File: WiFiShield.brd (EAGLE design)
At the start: 69.2 x 53.3 mm, 39 parts, among them IC1 MIC5219-3.3YM5, IC2 CC3000, J7 Arduino-compatible headers, Q1 2N7002, Q2 2N7002, Q3 2N7002, Q4 2N7002, Q5 2N7002

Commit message: foo
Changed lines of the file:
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@@
 <via x="33.02" y="39.37" extent="1-16" drill="0.4"/>
 <wire x1="33.02" y1="39.37" x2="55.08625" y2="39.37" width="0.4064" layer="16"/>
-<wire x1="55.08625" y1="39.37" x2="56.67375" y2="37.7825" width="0.2032" layer="16"/>
+<wire x1="55.08625" y1="39.37" x2="56.67375" y2="37.7825" width="0.254" layer="16"/>
 <wire x1="57.045" y1="36.46" x2="57.045" y2="37.41125" width="0.2032" layer="1"/>
 <wire x1="57.045" y1="37.41125" x2="56.67375" y2="37.7825" width="0.2032" layer="1"/>
@@
 <wire x1="39.6875" y1="41.5425" x2="39.685" y2="41.545" width="0.4064" layer="1"/>
 <wire x1="39.497" y1="39.37" x2="56.67375" y2="39.37" width="0.4064" layer="1"/>
-<wire x1="56.67375" y1="39.37" x2="58.245" y2="37.79875" width="0.2032" layer="16"/>
+<wire x1="56.67375" y1="39.37" x2="58.245" y2="37.79875" width="0.254" layer="16"/>
 <wire x1="58.245" y1="36.46" x2="58.245" y2="37.79875" width="0.2032" layer="1"/>
 <via x="56.67375" y="39.37" extent="1-16" drill="0.4"/>

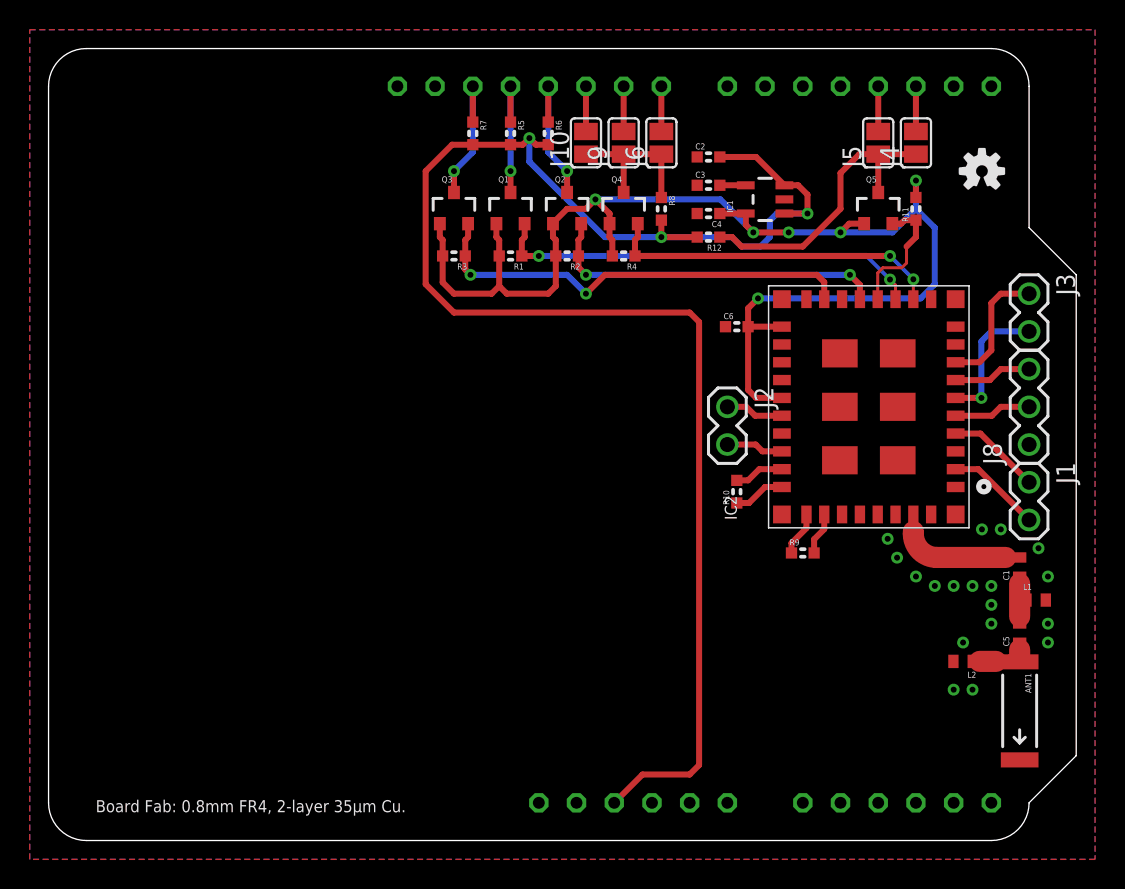
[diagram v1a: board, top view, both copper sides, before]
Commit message: finished silkscreen
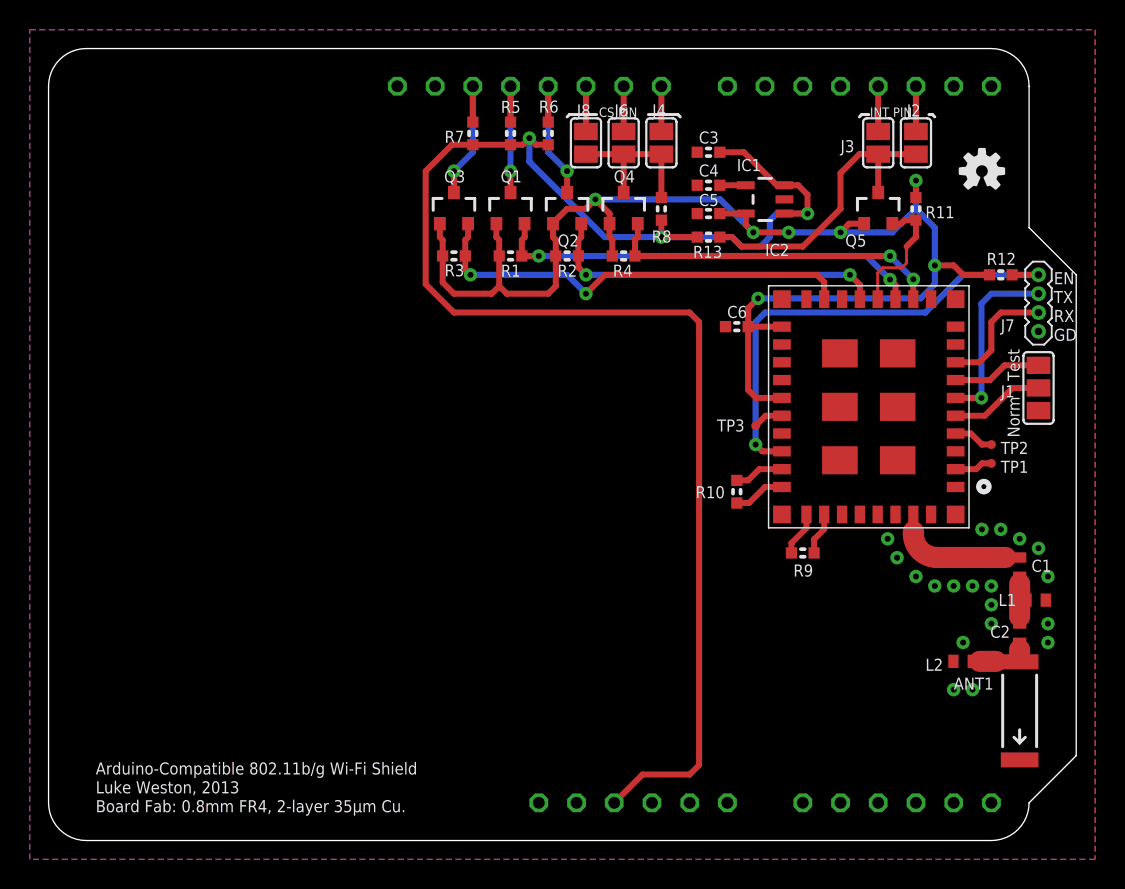
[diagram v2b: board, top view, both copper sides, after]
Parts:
- removed J10, J9: (no value), freetronics-luke:SJ
- added R13: 10kΩ, freetronics-master-v1:0603
- added TP1, TP2, TP3: (no value), testpad:TP06R
- C2: value 2.2µF -> 2.2pF; device freetronics-master-v1:0603 -> freetronics-master-v1:C0402
- C3: value 470pF -> 2.2µF
- C4: value 2.2µF -> 470pF
- C5: value 2.2pF -> 2.2µF; device freetronics-master-v1:C0402 -> freetronics-master-v1:0603
- IC1: value MIC5219-3.3YM5 -> MIC5219
- J1: value (none) -> Mode; device freetronics-master-v1:1X02 -> freetronics-master-v1:SJ_2
- J2, J3: device freetronics-master-v1:1X02 -> freetronics-luke:SJ
- J5: value (none) -> Arduino-compatible headers; device freetronics-luke:SJ -> Arduino-Various:NO-OUTLINE-OCTAGONAL-NOTEXT
- J7: value Arduino-compatible headers -> (none); device Arduino-Various:NO-OUTLINE-OCTAGONAL-NOTEXT -> freetronics-master-v1:1X04-1.27MM
- J8: device freetronics-master-v1:1X03 -> freetronics-luke:SJ
- moved C2 38.3 mm to (65.4, 14.0), turned to 90 degrees
- moved J8 36.1 mm to (36.2, 47.0)
- moved C5 35.2 mm to (44.5, 42.2), turned to 180 degrees
- moved J7 33.6 mm to (66.7, 38.1)
- moved J5 29.6 mm to (35.6, 25.4), turned to 270 degrees
- moved J2 21.8 mm to (58.4, 47.0), turned to 90 degrees
- moved R12 19.8 mm to (64.1, 38.1)
- moved J4 17.1 mm to (41.3, 47.0)
- moved J3 14.4 mm to (55.9, 47.0), turned to 90 degrees
- moved J1 6.38 mm to (66.7, 30.5), turned to 90 degrees
- moved J6 2.54 mm to (38.7, 47.0)
- moved C3 2.22 mm to (44.5, 46.4)
- moved C4 1.91 mm to (44.5, 44.1), turned to 0 degrees
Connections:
- net !CC3000_CS_5V: now also J4.1, J8.1; no longer J10.1, J9.1
- net +3V3: now also C5.1, R12.2; no longer C4.1
- net +5V: now also C3.2, J5.5V, R13.2; no longer C2.2, J7.5V, R12.2
- net 3V3: now also J5.3V3; no longer J7.3V3
- net CC3000_EN: now also J7.1, R12.1; no longer J2.2
- net CC3000_IRQ_5V: now also J2.1, J3.1, R13.1; no longer J4.1, J5.1, R12.1
- net GND: now also C4.1, C5.2, J1.1, J5.GND0, J5.GND1, J5.GND2, J7.4; no longer C2.1, C4.2, J7.GND0, J7.GND1, J7.GND2, J8.1
- net MISO_5V: now also J5.12; no longer J7.12
- net MOSI_5V: now also J5.11; no longer J7.11
- net N$103: now also C2.2; no longer C5.2
- net N$104: now also C2.1; no longer C5.1
- net N$11: now also J5.10, J8.2; no longer J10.2, J7.10
- net N$4: now also J3.2, J5.3; no longer J5.2, J7.3
- net N$43: now also C4.2; no longer C3.2
- net N$6: now also J2.2, J5.2; no longer J4.2, J7.2
- net N$7: now also J5.9, J6.2; no longer J7.9, J9.2
- net N$9: now also J4.2, J5.8; no longer J6.2, J7.8
- net RES_1: now also TP1.TP; no longer J1.2
- net RES_2: now also TP2.TP; no longer J1.1
- net RES_3: now also TP3.TP; no longer J2.1
- net SCK_5V: now also J5.13; no longer J7.13
- net VIN: now also J5.VIN; no longer J7.VIN
- net WL_EN1: now also J1.3; no longer J8.3
- net WL_EN2: now also J1.2; no longer J8.2
- net WL_UART_RX: now also J7.3; no longer J3.1
- net WL_UART_TX: now also J7.2; no longer J3.2
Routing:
- net CC3000_EN: track 3.87 -> 32.4 mm, vias 0 -> 1
- net +3V3: track 89.4 -> 93.4 mm, vias 6 -> 7
- net RES_1: track 6.36 -> 2.57 mm
- net RES_2: track 6.30 -> 2.71 mm
- net WL_UART_TX: track 9.03 -> 12.2 mm
- net RES_3: track 3.92 -> 2.05 mm
- net WL_EN2: track 5.19 -> 6.35 mm
- net WL_EN1: track 5.25 -> 5.99 mm
- net WL_UART_RX: track 8.72 -> 8.08 mm
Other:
- board text added: "Arduino-Compatible 802.11b/g Wi-Fi Shield"
- board text added: "CS PIN"
- board text added: "EN"
- board text added: "GD"
- board text added: "INT PIN"
- board text added: "Luke Weston, 2013"
- board text added: "Norm"
- board text added: "RX"
- board text added: "TX"
- board text added: "Test"

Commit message: tweaked RF layout
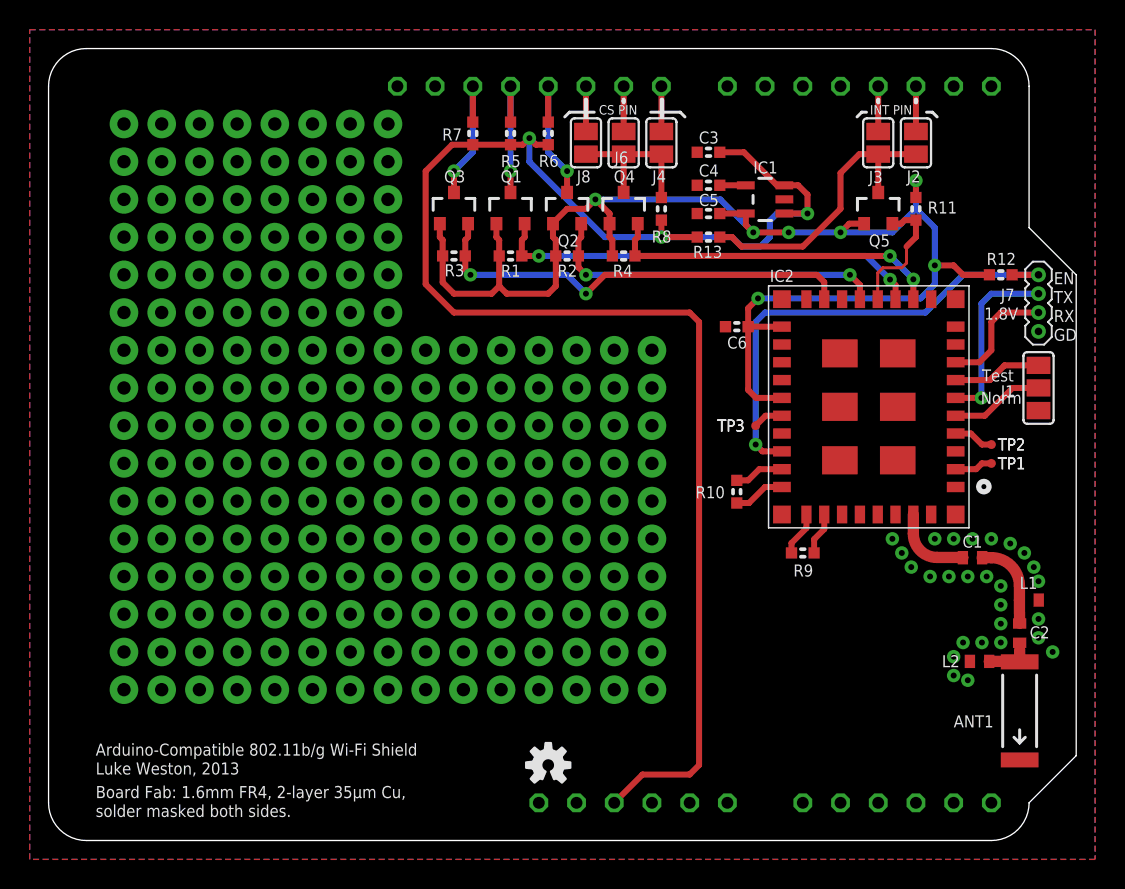
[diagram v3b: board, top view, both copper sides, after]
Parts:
- moved SY 49.5 mm to (33.7, 5.08)
- moved C1 3.24 mm to (62.2, 19.1), turned to 180 degrees
- moved L2 1.11 mm to (62.7, 12.1)
- moved L1 0.48 mm to (66.0, 16.2)
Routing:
- net N$16: track 9.12 -> 5.31 mm
- net N$104: track 5.83 -> 4.00 mm
- net N$103: track 4.45 -> 5.83 mm
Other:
- board text added: "1.8V"
- board text added: "Board Fab: 1.6mm FR4, 2-layer 35µm Cu,"
- board text added: "TP1"
- board text added: "TP2"
- board text added: "TP3"
- board text added: "solder masked both sides."
- board text removed: "Board Fab: 0.8mm FR4, 2-layer 35µm Cu."

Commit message: changed to microstrip antenna, fixed 50Ω line
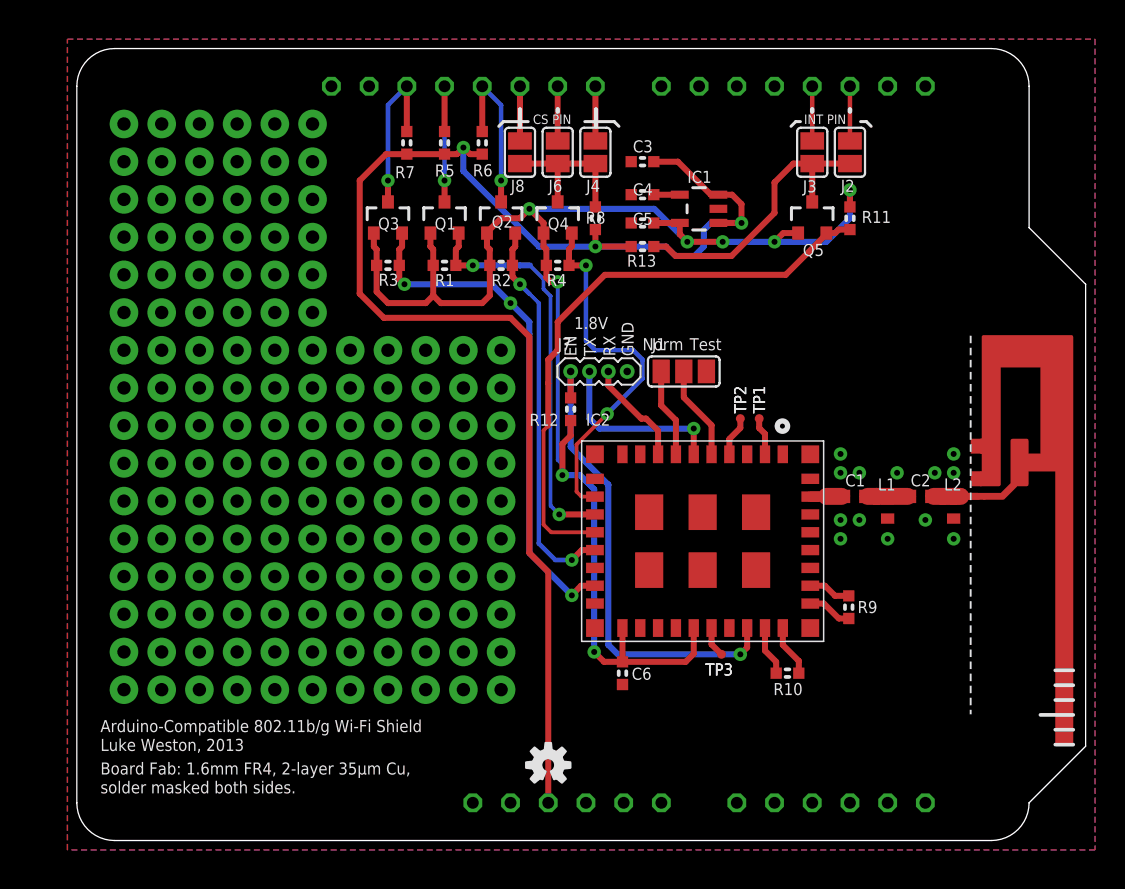
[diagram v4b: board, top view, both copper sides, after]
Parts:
- removed ANT1: ANT-2.45-CHP-T, SparkFun:ANTENNA-CHIP5
- added A1: INVERTED_F_ANTENNA+2, antenna:DN007+2
- moved J7 32.2 mm to (35.2, 31.6), turned to 0 degrees
- moved R12 30.4 mm to (35.2, 29.1), turned to 270 degrees
- moved C6 24.6 mm to (38.7, 11.3), turned to 90 degrees
- moved J1 23.9 mm to (42.8, 31.6), turned to 180 degrees
- moved TP2 17.0 mm to (46.6, 28.4), turned to 90 degrees
- moved TP1 15.9 mm to (47.9, 28.4), turned to 90 degrees
- moved TP3 15.6 mm to (45.3, 12.5), turned to 90 degrees
- moved IC2 14.4 mm to (44.1, 20.2), turned to 270 degrees
- moved R10 12.7 mm to (49.8, 11.3), turned to 180 degrees
- moved C2 11.4 mm to (58.7, 23.2), turned to 180 degrees
- moved L1 11.3 mm to (56.5, 22.3), turned to 270 degrees
- moved L2 10.4 mm to (61.0, 22.3), turned to 270 degrees
- moved C1 8.95 mm to (54.3, 23.2)
- moved R9 4.79 mm to (53.9, 15.7), turned to 90 degrees
- moved J2 4.49 mm to (54.0, 46.4)
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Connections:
- net GND: now also A1.GND, A1.GND@1
- net N$104: now also A1.FEED; no longer ANT1.FEED
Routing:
- net CC3000_IRQ_3.3V: track 8.82 -> 40.0 mm
- net +5V: track 110.8 -> 99.3 mm
- net +3V3: track 93.4 -> 103.8 mm, vias 7 -> 8
- net SCK_3.3V: track 29.9 -> 34.6 mm, vias 2 -> 3
- net N$16: track 5.31 -> 2.35 mm
- net MOSI_3.3V: track 23.4 -> 26.2 mm
- net MISO_3.3V: track 29.2 -> 27.2 mm
- net !CC3000_CS_3.3V: track 23.0 -> 24.9 mm
- net N$104: track 4.00 -> 5.91 mm
- net MOSI_5V: track 10.1 -> 11.4 mm
- net SCK_5V: track 10.1 -> 11.4 mm
- net MISO_5V: track 9.57 -> 10.8 mm
- net N$40: track 0.00 -> 1.03 mm, vias 1 -> 0
- net WL_UART_RX: track 8.08 -> 7.15 mm
- net N$9: track 3.05 -> 3.81 mm
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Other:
- board size 69.2 x 53.3 mm -> 67.9 x 53.3 mm
- board text added: "GND"
- board text removed: "GD"
